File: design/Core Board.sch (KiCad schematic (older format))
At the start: 3 parts

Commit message: decide to put CPU on mainboard, drop core board design
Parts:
- removed P?: PP&Power, symbol CONN_8X2_CATSQUIRT
- removed P?: IOC&PB, symbol CONN_8X2_CATSQUIRT
- removed P?: PA&PAD, symbol CONN_8X2_CATSQUIRT
- added C? (x2): 22pF, symbol C
- added C?: 3.3nF, symbol C
- added C?: 100nF, symbol C
- added C?: 330pF, symbol C
- added C? (x5): .1uF, symbol C
- added C?: 104, symbol C
- added JP?: JUMPER, symbol JUMPER
- added P?: BDM, symbol CONN_3X2
- added R?: 10M, symbol R
- added R?: 3.9K, symbol R
- added R? (x4): 10k, symbol R
- added R?: 4.7K, symbol R
- added R?: 100R, symbol R
- added R?: 1K, symbol R
- added SW?: SW_PUSH, symbol SW_PUSH
- added U?: MC9S12XDP512, symbol MC9S12XDP512
- added X?: CRYSTAL, symbol CRYSTAL
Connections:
- net labels added: +5V, BKGD, RESET
- net labels removed: +5V_SWITCHED, PA6, PB1, PB2, PB3, PT1
- wire segments 4 -> 101
- no-connect marks 18 -> 66
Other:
- note added: "BDM connector"
- note added: "PLL + CLK"
- note added: "Van and Vdd must meet each other at the 5v regulator, so digital currents dont mess with the ADC stability.\nAlso, keep an analog ground plane beneath this Van track."
- note added: "manual reset switch"
- note added: "small pin change to prevent reverse polarity"

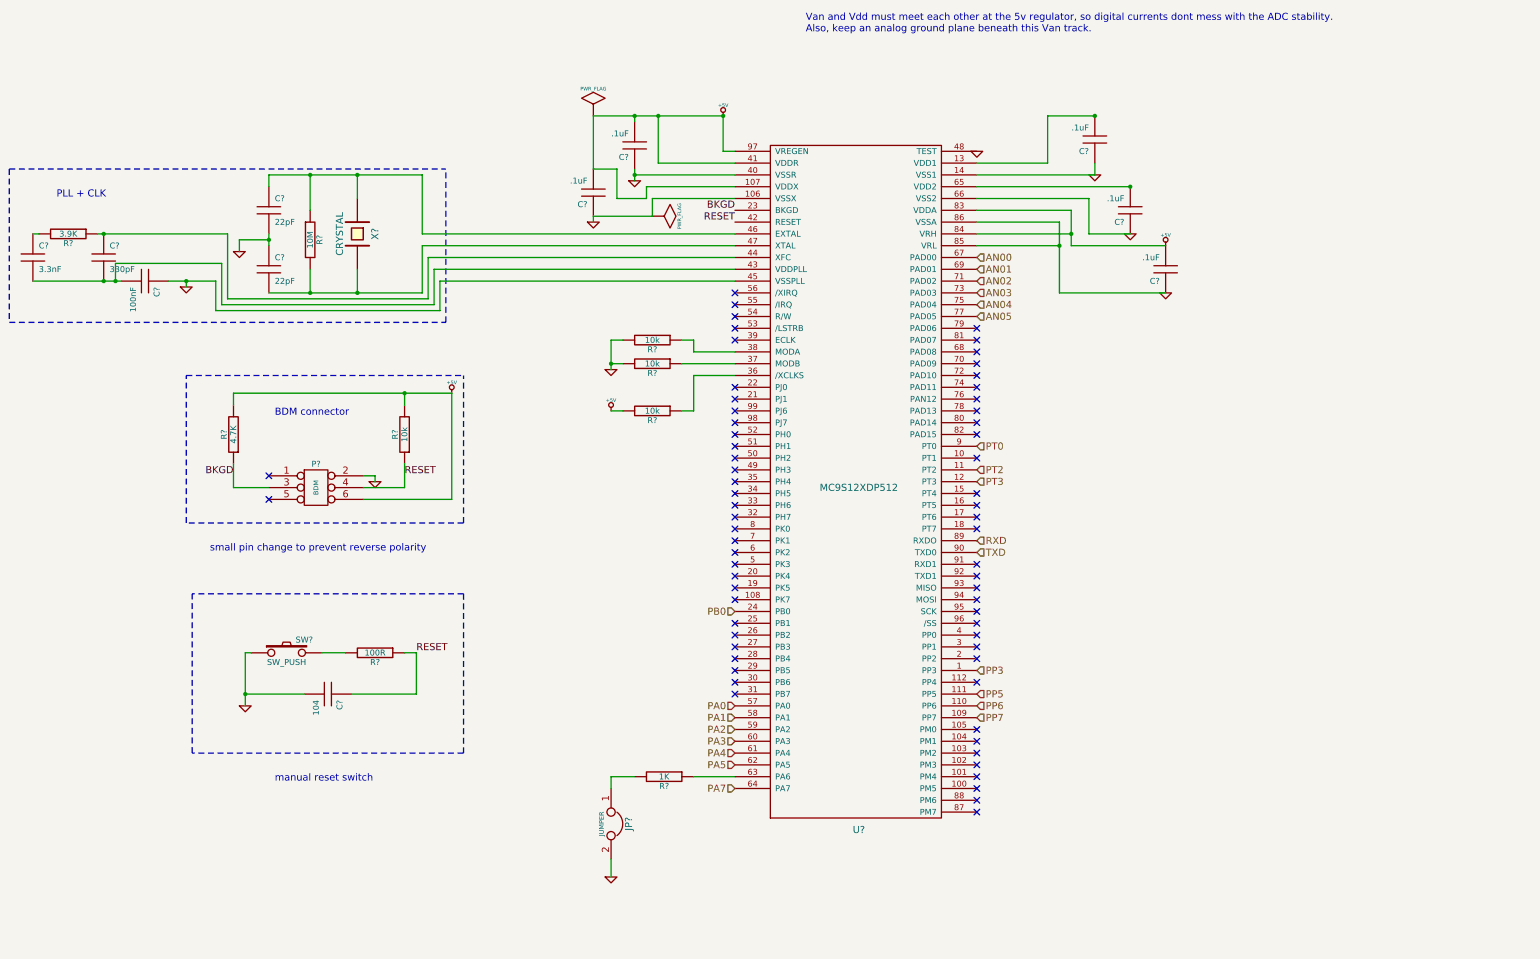
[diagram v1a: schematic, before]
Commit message: revise schema to be full pin compatible with stock ECU
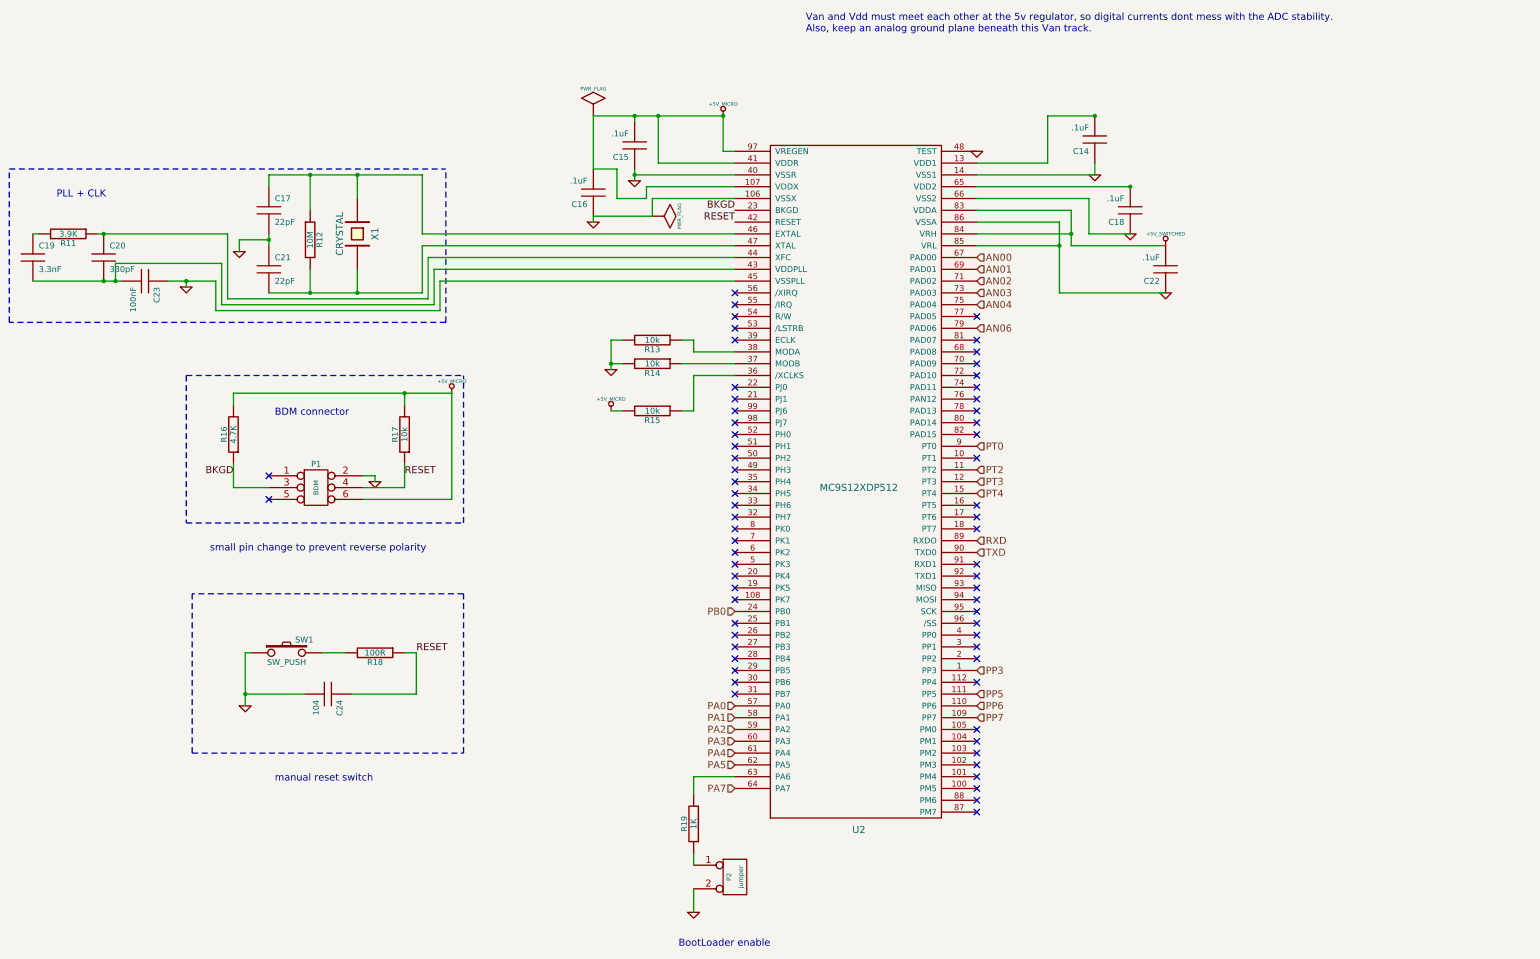
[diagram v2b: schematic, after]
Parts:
- removed JP?: JUMPER, symbol JUMPER
- added P2: jumper, symbol CONN_2
- gave numbers to parts that had none: 24
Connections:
- net GND: now also P2.2 (PM)
- net PT4: now reaches U2.15 (PT4)
- net at U2.63 (PA6): now also R19.2; no longer R19.1
- net AN06: now reaches U2.79 (PAD06)
- net +5V renamed +5V_MICRO
- net +5V_MICRO: no longer C22.2, U2.83 (VDDA), U2.84 (VRH)
- net AN05: no longer names the net of U2.77 (PAD05)
- new net: P2.1 (P1), R19.1
- new net +5V_SWITCHED: C22.2, U2.83 (VDDA), U2.84 (VRH)
- no-connect marks 66 -> 65
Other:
- note added: "BootLoader enable"
- moved on the sheet: R19

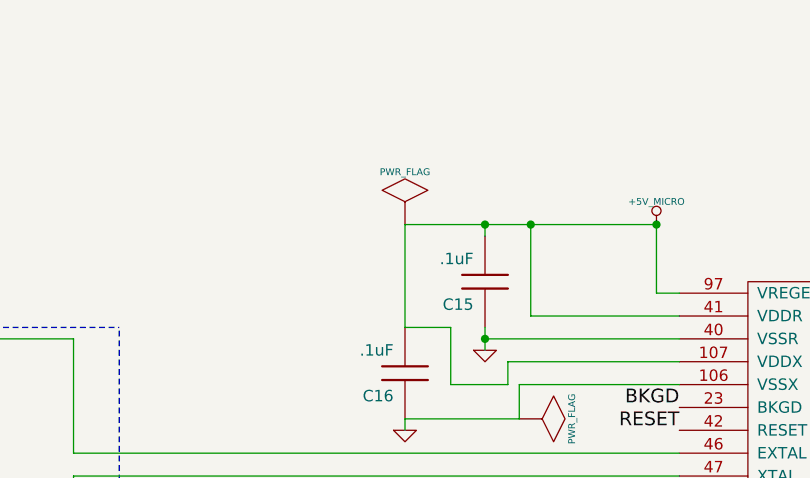
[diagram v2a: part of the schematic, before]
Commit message: add test points on critical output, resolve all kind of DRC issue, generate a netlist
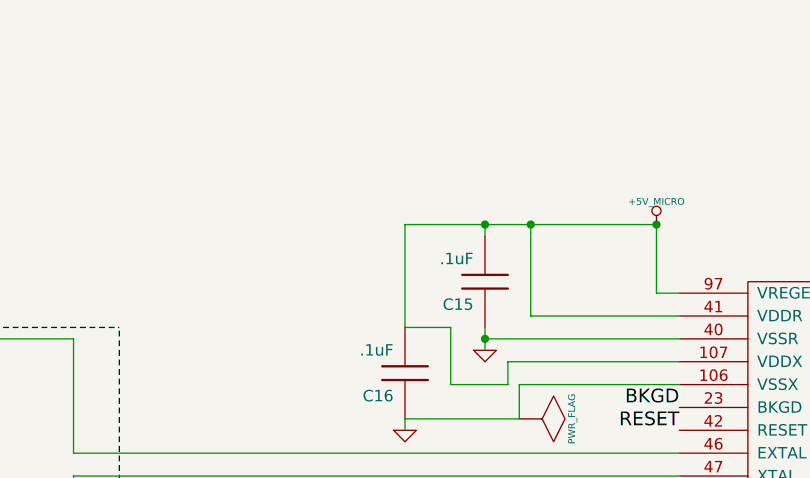
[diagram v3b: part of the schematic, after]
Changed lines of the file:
@@
-EESchema Schematic File Version 2  date 02/01/2012 14:25:41
+EESchema Schematic File Version 2  date 03/01/2012 09:04:48
 LIBS:power
 LIBS:device
@@
 Sheet 3 12
 Title "core"
-Date "2 jan 2012"
+Date "3 jan 2012"
 Rev "0.01"
 Comp "diyefi.org"
@@
 $EndDescr
 $Comp
-L +5V_SWITCHED #PWR018
+L PWR_FLAG #FLG1
+U 1 1 4EF89402
+P 7900 3700
+F 0 "#FLG1" H 7900 3970 30  0001 C CNN
+F 1 "PWR_FLAG" H 7900 3930 30  0000 C CNN
+	1    7900 3700
+	0    1    1    0
+$EndComp
+$Comp
+L +5V_SWITCHED #PWR26
 U 1 1 4EFBB324
 P 12250 3950
-F 0 "#PWR018" H 12250 3900 20  0001 C CNN
+F 0 "#PWR26" H 12250 3900 20  0001 C CNN
 F 1 "+5V_SWITCHED" H 12250 4050 30  0000 C CNN
 	1    12250 3950
@@
 Connection ~ 8500 2850
 $Comp
-L +5V_MICRO #PWR019
+L +5V_MICRO #PWR31
 U 1 1 4EFB34CE
 P 6200 5200
-F 0 "#PWR019" H 6200 5150 20  0001 C CNN
+F 0 "#PWR31" H 6200 5150 20  0001 C CNN
 F 1 "+5V_MICRO" H 6200 5300 30  0000 C CNN
 	1    6200 5200
@@
 $EndComp
 $Comp
-L +5V_MICRO #PWR020
+L +5V_MICRO #PWR32
 U 1 1 4EFB34CB
 P 7550 5350
-F 0 "#PWR020" H 7550 5300 20  0001 C CNN
+F 0 "#PWR32" H 7550 5300 20  0001 C CNN
 F 1 "+5V_MICRO" H 7550 5450 30  0000 C CNN
 	1    7550 5350
@@
 $EndComp
 $Comp
-L +5V_MICRO #PWR021
+L +5V_MICRO #PWR20
 U 1 1 4EFB34C6
 P 8500 2850
-F 0 "#PWR021" H 8500 2800 20  0001 C CNN
+F 0 "#PWR20" H 8500 2800 20  0001 C CNN
 F 1 "+5V_MICRO" H 8500 2950 30  0000 C CNN
 	1    8500 2850
@@
 PT4
 $Comp
-L GND #PWR022
+L GND #PWR35
 U 1 1 4EF8A1A8
 P 8250 9600
-F 0 "#PWR022" H 8250 9600 30  0001 C CNN
+F 0 "#PWR35" H 8250 9600 30  0001 C CNN
 F 1 "GND" H 8250 9530 30  0001 C CNN
 	1    8250 9600
@@
 RESET
 $Comp
-L GND #PWR023
+L GND #PWR34
 U 1 1 4EF89428
 P 4450 7850
-F 0 "#PWR023" H 4450 7850 30  0001 C CNN
+F 0 "#PWR34" H 4450 7850 30  0001 C CNN
 F 1 "GND" H 4450 7780 30  0001 C CNN
 	1    4450 7850
@@
 NoConn ~ 4650 6100
 $Comp
-L GND #PWR024
+L GND #PWR33
 U 1 1 4EF89423
 P 5550 5950
-F 0 "#PWR024" H 5550 5950 30  0001 C CNN
+F 0 "#PWR33" H 5550 5950 30  0001 C CNN
 F 1 "GND" H 5550 5880 30  0001 C CNN
 	1    5550 5950
@@
 $EndComp
 $Comp
-L GND #PWR025
+L GND #PWR22
 U 1 1 4EF89421
 P 11650 3350
-F 0 "#PWR025" H 11650 3350 30  0001 C CNN
+F 0 "#PWR22" H 11650 3350 30  0001 C CNN
 F 1 "GND" H 11650 3280 30  0001 C CNN
 	1    11650 3350
@@
 $EndComp
 $Comp
-L GND #PWR026
+L GND #PWR25
 U 1 1 4EF89420
 P 11950 3850
-F 0 "#PWR026" H 11950 3850 30  0001 C CNN
+F 0 "#PWR25" H 11950 3850 30  0001 C CNN
 F 1 "GND" H 11950 3780 30  0001 C CNN
 	1    11950 3850
@@
 $EndComp
 $Comp
-L GND #PWR027
+L GND #PWR29
 U 1 1 4EF8941F
 P 12250 4350
-F 0 "#PWR027" H 12250 4350 30  0001 C CNN
+F 0 "#PWR29" H 12250 4350 30  0001 C CNN
 F 1 "GND" H 12250 4280 30  0001 C CNN
 	1    12250 4350
@@
 $EndComp
 $Comp
-L GND #PWR028
+L GND #PWR23
 U 1 1 4EF8941E
 P 7750 3400
-F 0 "#PWR028" H 7750 3400 30  0001 C CNN
+F 0 "#PWR23" H 7750 3400 30  0001 C CNN
 F 1 "GND" H 7750 3330 30  0001 C CNN
 	1    7750 3400
@@
 $EndComp
 $Comp
-L GND #PWR029
+L GND #PWR24
 U 1 1 4EF8941D
 P 7400 3750
-F 0 "#PWR029" H 7400 3750 30  0001 C CNN
+F 0 "#PWR24" H 7400 3750 30  0001 C CNN
 F 1 "GND" H 7400 3680 30  0001 C CNN
 	1    7400 3750
@@
 $EndComp
 $Comp
-L GND #PWR030
+L GND #PWR21
 U 1 1 4EF8941A
 P 10650 3150
-F 0 "#PWR030" H 10650 3150 30  0001 C CNN
+F 0 "#PWR21" H 10650 3150 30  0001 C CNN
 F 1 "GND" H 10650 3080 30  0001 C CNN
 	1    10650 3150
@@
 $EndComp
 $Comp
-L GND #PWR031
+L GND #PWR30
 U 1 1 4EF89415
 P 7550 5000
-F 0 "#PWR031" H 7550 5000 30  0001 C CNN
+F 0 "#PWR30" H 7550 5000 30  0001 C CNN
 F 1 "GND" H 7550 4930 30  0001 C CNN
 	1    7550 5000
@@
 PLL + CLK
 $Comp
-L GND #PWR032
+L GND #PWR28
 U 1 1 4EF89410
 P 3950 4300
-F 0 "#PWR032" H 3950 4300 30  0001 C CNN
+F 0 "#PWR28" H 3950 4300 30  0001 C CNN
 F 1 "GND" H 3950 4230 30  0001 C CNN
 	1    3950 4300
@@
 $EndComp
 $Comp
-L GND #PWR033
+L GND #PWR27
 U 1 1 4EF8940F
 P 4400 4000
-F 0 "#PWR033" H 4400 4000 30  0001 C CNN
+F 0 "#PWR27" H 4400 4000 30  0001 C CNN
 F 1 "GND" H 4400 3930 30  0001 C CNN
 	1    4400 4000
@@
 NoConn ~ 10650 7050
 $Comp
-L PWR_FLAG #FLG034
-U 1 1 4EF89403
-P 7400 2850
-F 0 "#FLG034" H 7400 3120 30  0001 C CNN
-F 1 "PWR_FLAG" H 7400 3080 30  0000 C CNN
-	1    7400 2850
-	1    0    0    -1
-$EndComp
-$Comp
-L PWR_FLAG #FLG035
-U 1 1 4EF89402
-P 7900 3700
-F 0 "#FLG035" H 7900 3970 30  0001 C CNN
-F 1 "PWR_FLAG" H 7900 3930 30  0000 C CNN
-	1    7900 3700
-	0    1    1    0
-$EndComp
-$Comp
 L MC9S12XDP512 U2
